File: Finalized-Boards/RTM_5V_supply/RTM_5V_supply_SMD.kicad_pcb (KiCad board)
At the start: 4 copper layers, 18.5 x 99 mm, 15 parts, among them J1 86093968114755V1LF

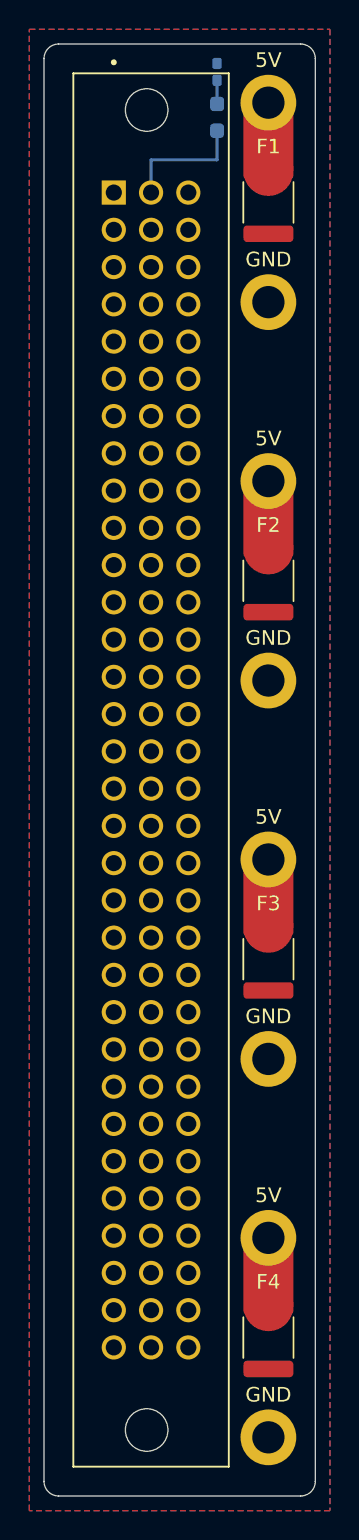
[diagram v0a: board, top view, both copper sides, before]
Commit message: Matt's 9/17 review: RTM paired 5V/GND terminals, SRAM R1/R2 to 0603, fanout per-destination polyswitches; archive 9/16 boards
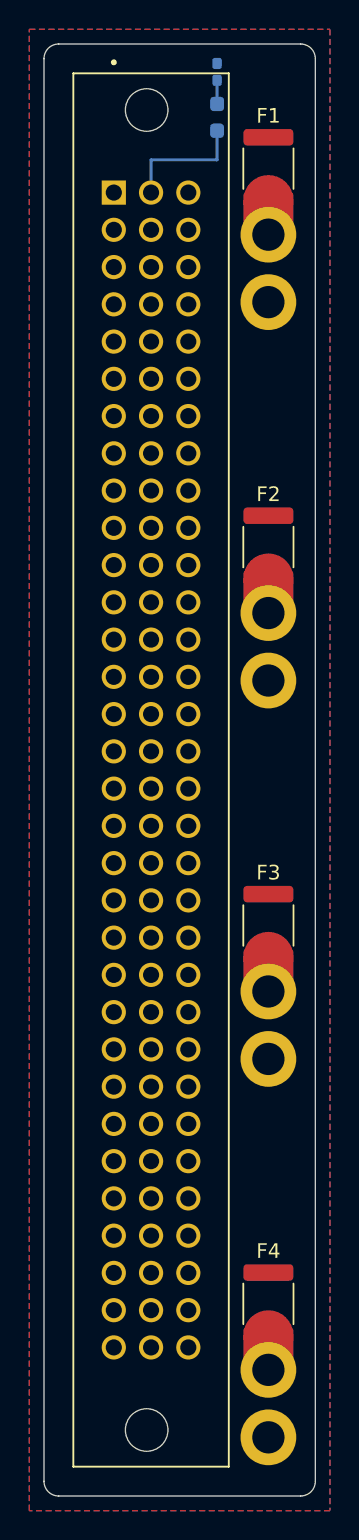
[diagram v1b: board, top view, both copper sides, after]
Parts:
- +5VP1, +5VP2, +5VP3, +5VP4, GND1, GND2, GND3, GND4: moved to B.Cu
- moved +5VP1 9.00 mm to (108.0, 63.5)
- moved +5VP2 9.00 mm to (108.0, 89.3)
- moved +5VP3 9.00 mm to (108.0, 115.1)
- moved +5VP4 9.00 mm to (108.0, 140.9)
- moved F3 2.30 mm to (108.0, 110.6), turned to -90 degrees
- moved F1 2.30 mm to (108.0, 59.0), turned to -90 degrees
- moved F2 2.30 mm to (108.0, 84.8), turned to -90 degrees
- moved F4 2.30 mm to (108.0, 136.4), turned to -90 degrees
- turned GND1 to 180 degrees
- turned GND2 to 180 degrees
- turned GND3 to 180 degrees
- turned GND4 to 180 degrees
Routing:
- net Net-(+5VP3-Pad1): track 4.66 -> 2.36 mm
- net Net-(+5VP2-Pad1): track 4.66 -> 2.36 mm
- net Net-(+5VP1-Pad1): track 4.66 -> 2.36 mm
- net Net-(+5VP4-Pad1): track 4.66 -> 2.36 mm
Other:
- board text removed: "5V"
- board text removed: "F1"
- board text removed: "F2"
- board text removed: "F3"
- board text removed: "F4"
- board text removed: "GND"

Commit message: Polyswitches sized to load: RTM F1-F4 MF-MSMF110/16-2 -> MF-MSMF030-2 (0.3 A), fanout F1-F4 -> MF-MSMF010-2 (0.1 A); refresh renders and DRC
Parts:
- F1, F2, F3, F4: value MF-MSMF110/16-2 -> MF-MSMF030-2
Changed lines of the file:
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@@
 			)
 		)
-		(property "Value" "MF-MSMF110/16-2"
+		(property "Value" "MF-MSMF030-2"
 			(at 0 2.65 90)
 			(layer "F.Fab")
@@
 			)
 		)
-		(property "Value" "MF-MSMF110/16-2"
+		(property "Value" "MF-MSMF030-2"
 			(at 0 2.65 90)
 			(layer "F.Fab")
@@
 			)
 		)
-		(property "Value" "MF-MSMF110/16-2"
+		(property "Value" "MF-MSMF030-2"
 			(at 0 2.65 90)
 			(layer "F.Fab")
@@
 			)
 		)
-		(property "Value" "MF-MSMF110/16-2"
+		(property "Value" "MF-MSMF030-2"
 			(at 0 2.65 90)
 			(layer "F.Fab")
@@
 	)
 	(segment
-		(start 108 86.9375)
-		(end 108 89.3)
-		(width 3.4)
-		(layer "F.Cu")
-		(net "Net-(+5VP2-Pad1)")
-	)
-	(segment
 		(start 104.5 58.4)
 		(end 100 58.4)
@@
 	)
 	(segment
+		(start 108 86.9375)
+		(end 108 89.3)
+		(width 3.4)
+		(layer "F.Cu")
+		(net "Net-(+5VP2-Pad1)")
+	)
+	(segment
